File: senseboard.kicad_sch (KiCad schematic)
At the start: 81 parts, among them J1 USB_C_Receptacle_USB2.0_16P, J2 Screw_Terminal_01x02, J3 DM3AT-SF-PEJM5, J4 Conn_01x04, J5 Conn_01x08, U1 USBLC6-2SC6, U2 TPS62840DLCR, U3 TPS62840DLCR, U4 SCD41-D-R2, U5 SGP41-D-R4, U6 SGP41-D-R4, U7 SHT4x, U8 STM32L4Q5CGUx, U9 RFM95W-915S2, Y1 Crystal_GND3

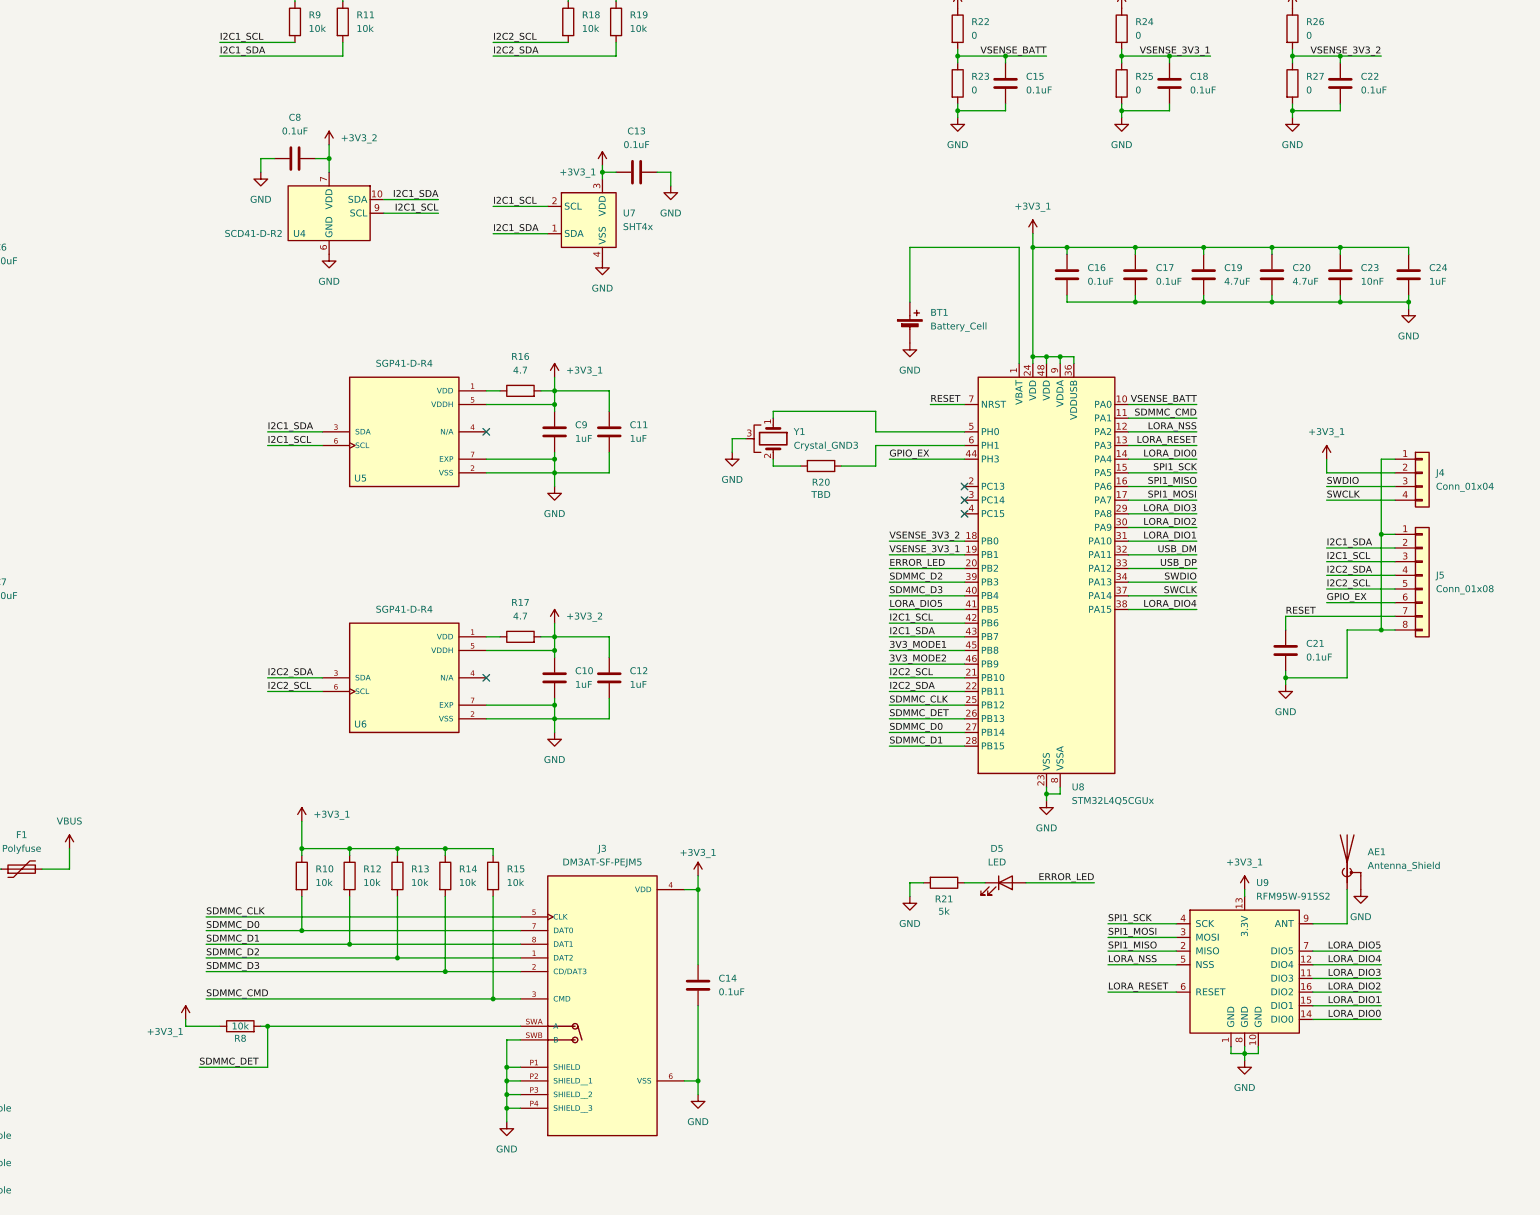
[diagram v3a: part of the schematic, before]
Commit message: added sd card protection, completed most layout, added bosch sensor, graphics
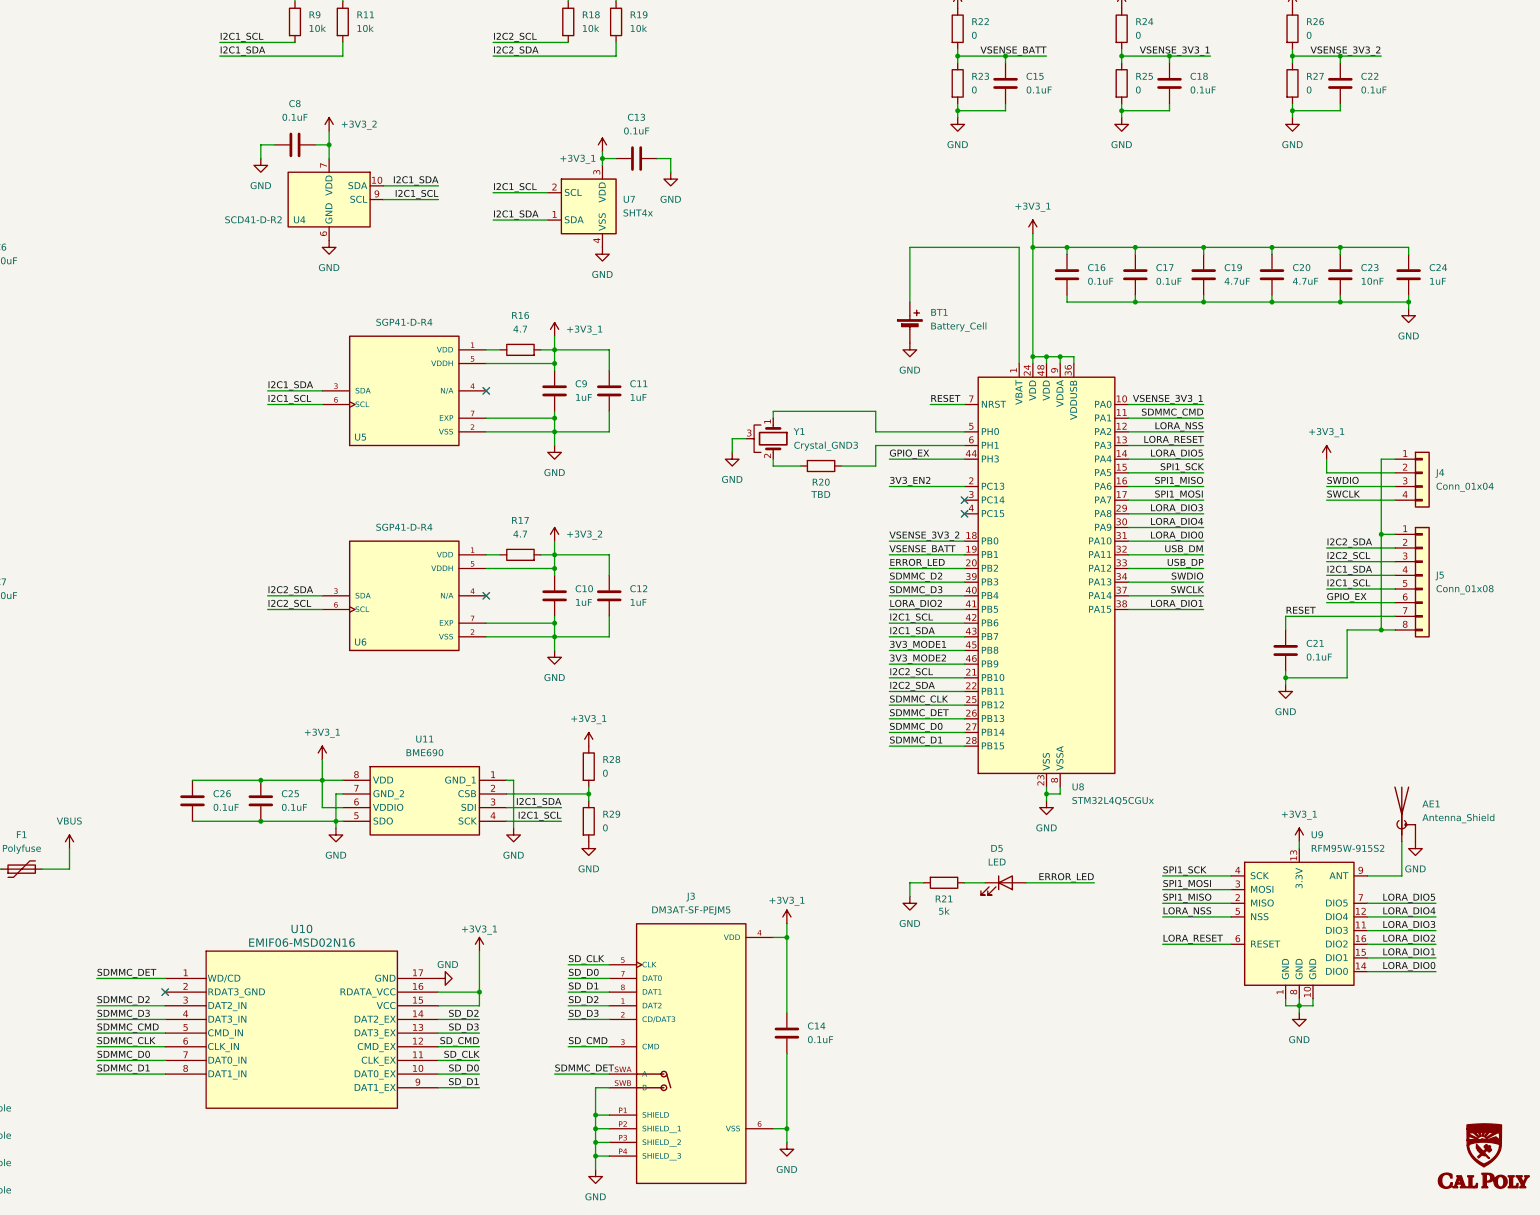
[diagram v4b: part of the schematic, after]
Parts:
- removed R10, R12, R13, R14, R15, R8: 10k, Resistor_SMD:R_0402_1005Metric, symbol Device:R
- added C25, C26: 0.1uF, Capacitor_SMD:C_0402_1005Metric, symbol Device:C
- added R28, R29: 0, Resistor_SMD:R_0402_1005Metric, symbol Device:R
- added U10: EMIF06-MSD02N16, EMIF06_MSD02N16:MICROQFN16_1P25X3P55X0P4_STM, symbol EMIF06_MSD02N16:EMIF06-MSD02N16
- added U11: BME690, BME690:BME690, symbol BME690:BME690
- C19, C20: footprint Capacitor_SMD:C_0805_2012Metric -> Capacitor_SMD:C_0603_1608Metric
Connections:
- net +3V3_1: now also C25.1, C26.1, R28.1, U10.15 (VCC), U10.16 (RDATA_VCC), U11.6 (VDDIO), U11.8 (VDD)
- net 3V3_EN2: now also U8.2 (PC13)
- net GND: now also C25.2, C26.2, R29.2, U10.17 (GND), U11.1 (GND_1), U11.5 (SDO), U11.7 (GND_2)
- net I2C1_SCL: now also J5.5 (Pin_5), U11.4 (SCK); no longer J5.3 (Pin_3)
- net I2C1_SDA: now also J5.4 (Pin_4), U11.3 (SDI); no longer J5.2 (Pin_2)
- net I2C2_SCL: now also J5.3 (Pin_3); no longer J5.5 (Pin_5)
- net I2C2_SDA: now also J5.2 (Pin_2); no longer J5.4 (Pin_4)
- net LORA_DIO0: now also U8.31 (PA10); no longer U8.14 (PA4)
- net LORA_DIO1: now also U8.38 (PA15); no longer U8.31 (PA10)
- net LORA_DIO2: now also U8.41 (PB5); no longer U8.30 (PA9)
- net LORA_DIO4: now also U8.30 (PA9); no longer U8.38 (PA15)
- net LORA_DIO5: now also U8.14 (PA4); no longer U8.41 (PB5)
- net SDMMC_CLK: now also U10.6 (CLK_IN); no longer J3.5 (CLK)
- net SDMMC_CMD: now also U10.5 (CMD_IN); no longer J3.3 (CMD)
- net SDMMC_D0: now also U10.7 (DAT0_IN); no longer J3.7 (DAT0)
- net SDMMC_D1: now also U10.8 (DAT1_IN); no longer J3.8 (DAT1)
- net SDMMC_D2: now also U10.3 (DAT2_IN); no longer J3.1 (DAT2)
- net SDMMC_D3: now also U10.4 (DAT3_IN); no longer J3.2 (CD/DAT3)
- net SDMMC_DET: now also U10.1 (WD/CD)
- net VSENSE_3V3_1: now also U8.10 (PA0); no longer U8.19 (PB1)
- net VSENSE_BATT: now also U8.19 (PB1); no longer U8.10 (PA0)
- new net: R28.2, R29.1, U11.2 (CSB)
- new net SD_CLK: J3.5 (CLK), U10.11 (CLK_EX)
- new net SD_CMD: J3.3 (CMD), U10.12 (CMD_EX)
- new net SD_D0: J3.7 (DAT0), U10.10 (DAT0_EX)
- new net SD_D1: J3.8 (DAT1), U10.9 (DAT1_EX)
- new net SD_D2: J3.1 (DAT2), U10.14 (DAT2_EX)
- new net SD_D3: J3.2 (CD/DAT3), U10.13 (DAT3_EX)
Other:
- moved on the sheet: AE1, C10, C11, C12, C13, C14, C8, C9, J3, R16, R17, U4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
